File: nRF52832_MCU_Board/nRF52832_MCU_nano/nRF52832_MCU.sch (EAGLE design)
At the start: 17 parts, among them U1 NRF52832, X1 32MHz, X2 TSW-116-02-S-S, X3 TSW-116-02-S-S

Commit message: Finished? footprint and symbol for nRF5, QFN. Done som experimenting on board layouts
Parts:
- removed X2, X3: TSW-116-02-S-S, con-samtec:TSW-116-02-S-S
- added ANT1: 2.45GHZ_PCB_ANTENNA, nRF:2.45GHZ_PCB_ANTENNA
- added C13: 0.8pF, rcl:C-EUC0402
- added J1, J2: TSW-116-02-S-S, con-samtec:TSW-116-02-S-S
- X1: device IQD-Frequency-Products:CRYSTALS-GND-LID-IQXC-42 -> nRF:XTAL_32MHZ
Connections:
- net N$1 renamed ANT
- new net N$1: ANT1.P$1, C13.1, L1.2
- new net N$14: U1.SWDIO@26
- new net N$15: U1.SWDCLK@25
- new net P0.00: J1-1.1, U1.P0.00/XL1@02
- new net P0.01: J1-2.1, U1.P0.01/XL2@03
- new net P0.02: J1-3.1, U1.P0.02/AIN0@04
- new net P0.03: J1-4.1, U1.P0.03/AIN1@05
- new net P0.04: J1-5.1, U1.P0.04/AIN2@06
- new net P0.05: J1-6.1, U1.P0.05/AIN3@07
- new net P0.06: J1-7.1, U1.P0.06@08
- new net P0.07: J1-8.1, U1.P0.07@09
- new net P0.08: J1-9.1, U1.P0.08@10
- new net P0.09: J1-10.1, U1.P0.09@11
- new net P0.10: J1-11.1, U1.P0.10@12
- new net P0.11: J1-12.1, U1.P0.11@14
- new net P0.12: J1-13.1, U1.P0.12@15
- new net P0.13: J1-14.1, U1.P0.13@16
- new net P0.14: J1-15.1, U1.P0.14@17
- new net P0.15: J1-16.1, U1.P0.15@18
- new net P0.16: J2-16.1, U1.P0.16@19
- new net P0.17: J2-15.1, U1.P0.17@20
- new net P0.18: J2-14.1, U1.P0.18@21
- new net P0.19: J2-13.1, U1.P0.19@22
- new net P0.20: J2-12.1, U1.P0.20@23
- new net P0.21: J2-11.1, U1.P0.21/RESET@24
- new net P0.22: J2-10.1, U1.P0.22@27
- new net P0.23: J2-9.1, U1.P0.23@28
- new net P0.24: J2-8.1, U1.P0.24@29
- new net P0.25: J2-7.1, U1.P0.25@37
- new net P0.26: J2-6.1, U1.P0.26@38
- new net P0.27: J2-5.1, U1.P0.27@39
- new net P0.28: J2-4.1, U1.P0.28@40
- new net P0.29: J2-3.1, U1.P0.29@41
- new net P0.30: J2-2.1, U1.P0.30@42
- new net P0.31: J2-1.1, U1.P0.31@43
- net GND: now also C13.2

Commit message: Routed gpio
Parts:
- added C14, C15: 300pF, nRF:CAPACITOR_0402_N
- added C16: 100nF, nRF:CAPACITOR_0402_N
- added C17, C18: 10µF, nRF:CAPACITOR_0603_N
- added C19: 100µF, nRF:CAPACITOR_0805_N
- added C20: (no value), nRF:CAPACITOR_0402_N
- added J3: MM8130-2600, nRF:MM8130-2600
- added J4: FPC_05P-RA-SMD, nRF:FPC_05P-RA-SMD
- added J5: DEBUG_CONNECTOR, nRF:DEBUG_CONNECTOR
- added L2: 10µH, nRF:INDUCTOR_0603_N
- added L3: 15nH, nRF:INDUCTOR_0402_N
- added R1, R2, R3, R4: 0R, nRF:RESISTOR_0402_N
- added U$2: TLV1117, nRF:TLV1117
- added X2: 32.768kHz, nRF:XTAL_32KHZ
- ANT1: value 2.45GHZ_PCB_ANTENNA -> ANTENNA_QUARTER-WAVE_MONOPOLE_MEANDERED_LEFT; device nRF:2.45GHZ_PCB_ANTENNA -> nRF:ANTENNA_QUARTER-WAVE_MONOPOLE_MEANDERED_LEFT
- C1, C11, C12, C2, C3, C4, C5, C6, C7, C8: device rcl:C-EUC0402 -> nRF:CAPACITOR_0402_N
- C10, C9: device rcl:C-EUC0603 -> nRF:CAPACITOR_0603_N
- C13: value 0.8pF -> (none); device rcl:C-EUC0402 -> nRF:CAPACITOR_0402_N
- L1: device nRF:INDUCTOR(0402) -> nRF:INDUCTOR_0402_N
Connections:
- net N$4 renamed X1
- removed net N$14: U1.SWDIO@26
- removed net N$15: U1.SWDCLK@25
- removed net P0.18: J2-14.1, U1.P0.18@21
- removed net P0.21: J2-11.1, U1.P0.21/RESET@24
- removed net VCC: C5.1, C8.1, C9.1, U1.VDD@13, U1.VDD@36, U1.VDD@48
- new net N$2: L2.2, L3.1
- new net N$4: L2.1, U1.DCC@47
- new net N$5: C13.1, J3.@IN, L1.2
- new net NFC1: C14.2, J4.2, R3.1, U1.P0.09/NFC1@11
- new net NFC2: C15.1, J4.4, R4.2, U1.P0.10/NFC2@12
- new net P0.18/SWO: J1-10.1, J5.10, U1.P0.18/SWO@21
- new net P0.21/RESET: J1-13.1, J5.6, U1.P0.21/RESET@24
- new net SWDCLK: J5.4, U1.SWDCLK@25
- new net SWDIO: J5.2, U1.SWDIO@26
- new net VCC_P3V3: C18.1, C19.1, C5.1, C8.1, C9.1, J5.1, U$2.OUT, U1.VDD@13, U1.VDD@36, U1.VDD@48
- new net VCC_P5V0: C16.1, C17.1, U$2.IN
- new net XL1: C11.2, R1.1, U1.P0.00/XL1@02, X2.1
- new net XL2: C12.2, R2.2, U1.P0.01/XL2@03, X2.2
- net DEC4: now also L3.2
- net GND: now also C11.1, C12.1, C14.1, C15.2, C16.2, C17.2, C18.2, C19.2, C20.2, J3.@GND, J5.3, J5.5, J5.9, U$2.GND
- net N$1: now also C20.1, J3.@OUT; no longer C13.1, L1.2
- net P0.00: now also J2-9.1, R1.2; no longer J1-1.1, U1.P0.00/XL1@02
- net P0.01: now also J2-8.1, R2.1; no longer J1-2.1, U1.P0.01/XL2@03
- net P0.02: now also J2-7.1; no longer J1-3.1
- net P0.03: now also J2-6.1; no longer J1-4.1
- net P0.04: now also J2-5.1; no longer J1-5.1
- net P0.05: now also J2-4.1; no longer J1-6.1
- net P0.06: now also J2-3.1; no longer J1-7.1
- net P0.07: now also J2-2.1; no longer J1-8.1
- net P0.08: now also J2-1.1; no longer J1-9.1
- net P0.09: now also J1-1.1, R3.2; no longer J1-10.1, U1.P0.09@11
- net P0.10: now also J1-2.1, R4.1; no longer J1-11.1, U1.P0.10@12
- net P0.11: now also J1-3.1; no longer J1-12.1
- net P0.12: now also J1-4.1; no longer J1-13.1
- net P0.13: now also J1-5.1; no longer J1-14.1
- net P0.14: now also J1-6.1; no longer J1-15.1
- net P0.15: now also J1-7.1; no longer J1-16.1
- net P0.16: now also J1-8.1; no longer J2-16.1
- net P0.17: now also J1-9.1; no longer J2-15.1
- net P0.19: now also J1-11.1; no longer J2-13.1
- net P0.20: now also J1-12.1; no longer J2-12.1
- net P0.22: now also J1-14.1; no longer J2-10.1
- net P0.23: now also J1-15.1; no longer J2-9.1
- net P0.24: now also J1-16.1; no longer J2-8.1
- net P0.25: now also J2-16.1; no longer J2-7.1
- net P0.26: now also J2-15.1; no longer J2-6.1
- net P0.27: now also J2-14.1; no longer J2-5.1
- net P0.28: now also J2-13.1; no longer J2-4.1
- net P0.29: now also J2-12.1; no longer J2-3.1
- net P0.30: now also J2-11.1; no longer J2-2.1
- net P0.31: now also J2-10.1; no longer J2-1.1
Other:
- note added: "Power supply"

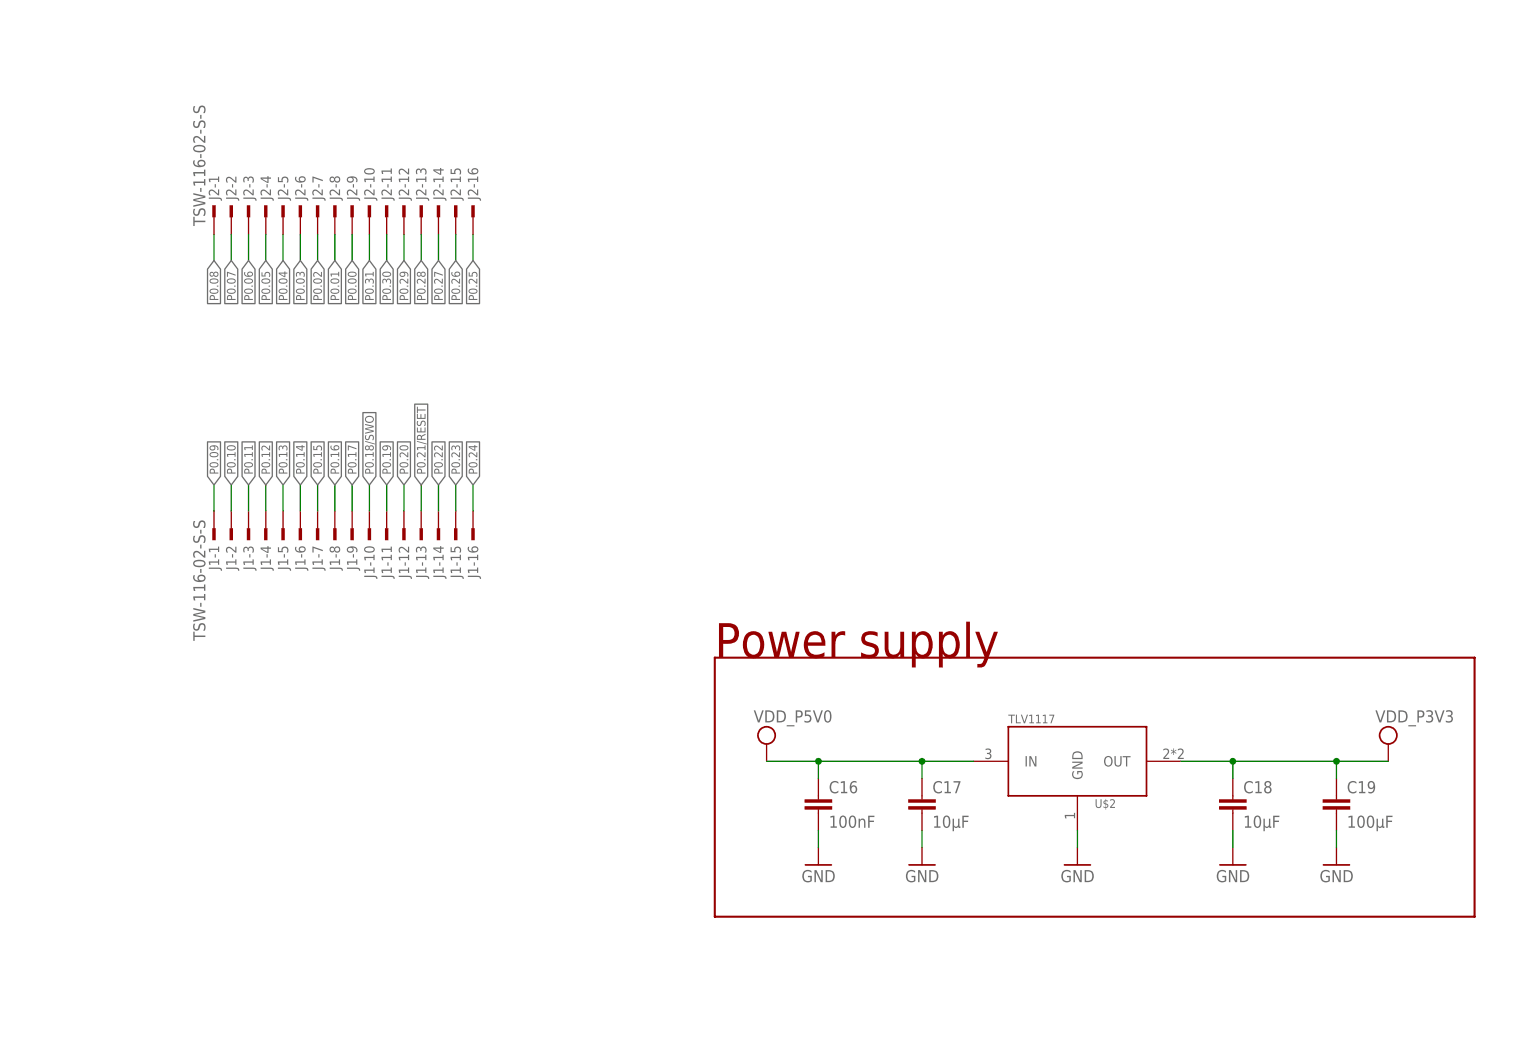
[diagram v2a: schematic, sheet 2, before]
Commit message: Positioned buttons, positioned powersupply
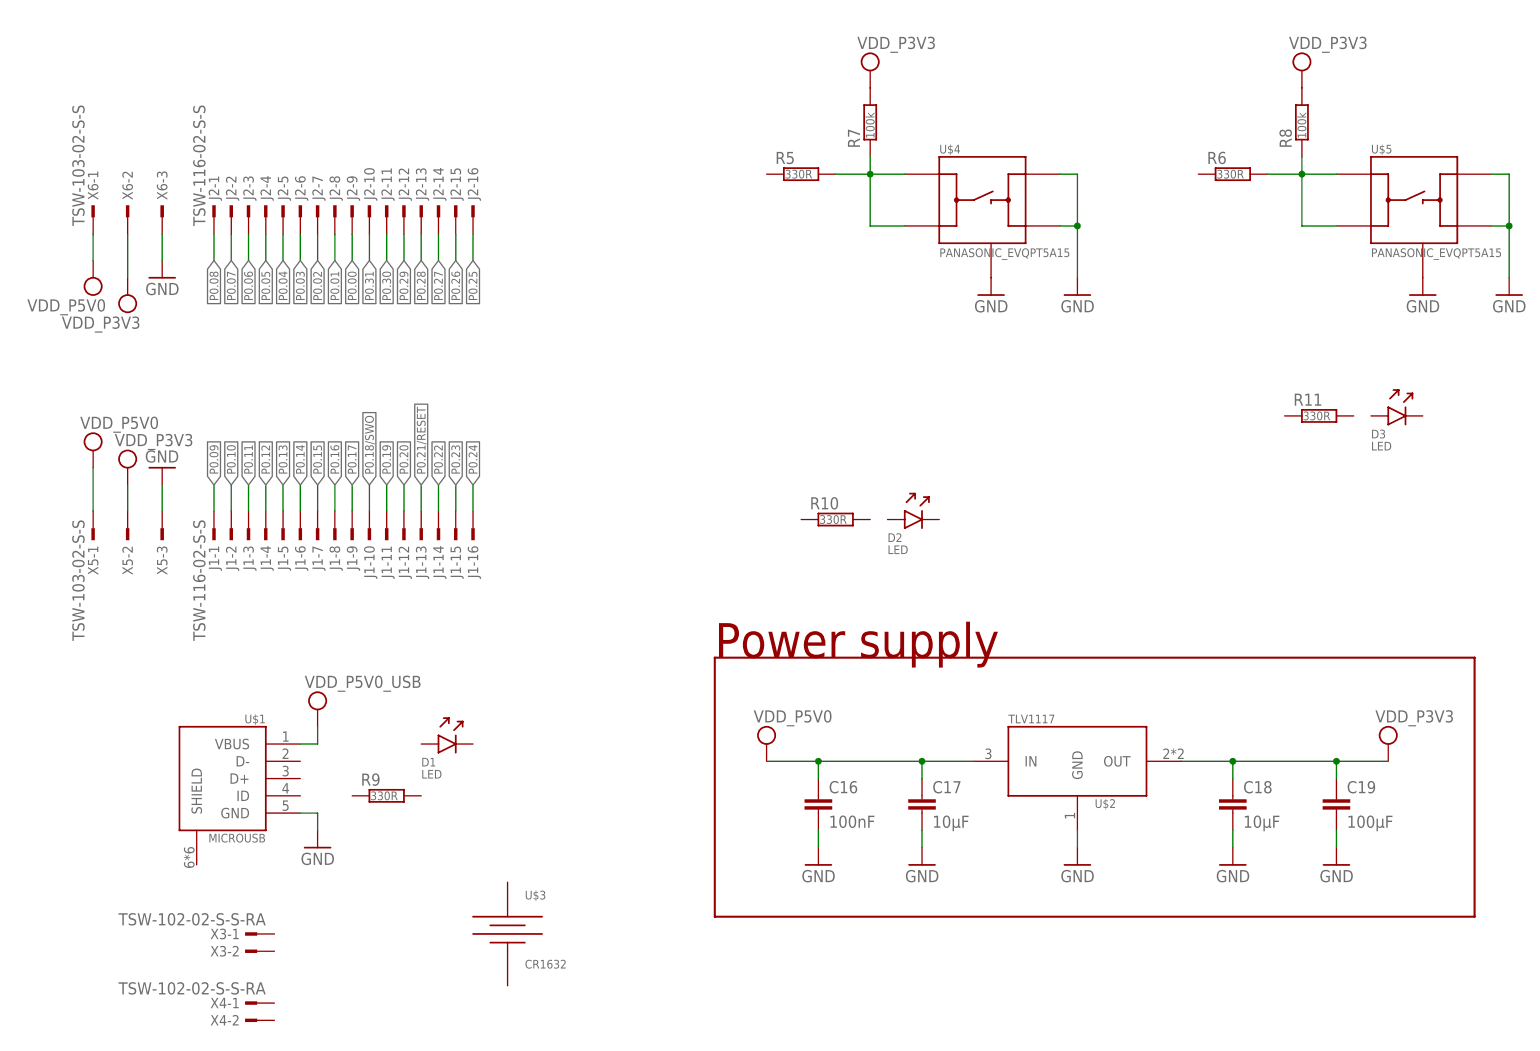
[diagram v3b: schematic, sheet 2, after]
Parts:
- added D1, D2, D3: LED, nRF:LED
- added R10, R11, R5, R6, R9: 330R, nRF:RESISTOR_0402_N
- added R7, R8: 100k, nRF:RESISTOR_0402_N
- added U$1: MICROUSB, nRF:MICROUSB
- added U$3: CR1632, nRF:CR1632
- added U$4, U$5: PANASONIC_EVQPT5A15, nRF:PANASONIC_EVQPT5A15
- added X3, X4: TSW-102-02-S-S-RA, con-samtec:TSW-102-02-S-S-RA
- added X5, X6: TSW-103-02-S-S, con-samtec:TSW-103-02-S-S
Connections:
- new net N$6: R6.2, R8.1, U$5.A, U$5.A'
- new net N$7: R5.2, R7.1, U$4.A, U$4.A'
- new net VCC: R7.2, R8.2
- new net VCC_P5V0_USB: U$1.VBUS
- net GND: now also U$1.GND, U$4.B, U$4.B', U$4.GND, U$5.B, U$5.B', U$5.GND, X5-3.1, X6-3.1
- net VCC_P3V3: now also X5-2.1, X6-2.1
- net VCC_P5V0: now also X5-1.1, X6-1.1
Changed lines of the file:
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@@
 <part name="C11" library="nRF" deviceset="CAPACITOR" device="_0402_N" value="12pF"/>
 <part name="C12" library="nRF" deviceset="CAPACITOR" device="_0402_N" value="12pF"/>
+<part name="U$1" library="nRF" deviceset="MICROUSB" device=""/>
+<part name="VDD_NRF6" library="supply2" deviceset="VCC" device="" value="VDD_P5V0_USB"/>
+<part name="GND22" library="supply1" deviceset="GND" device=""/>
+<part name="X3" library="con-samtec" deviceset="TSW-102-02-S-S" device="-RA"/>
+<part name="X4" library="con-samtec" deviceset="TSW-102-02-S-S" device="-RA"/>
+<part name="X5" library="con-samtec" deviceset="TSW-103-02-S-S" device=""/>
+<part name="X6" library="con-samtec" deviceset="TSW-103-02-S-S" device=""/>
+<part name="VDD_NRF7" library="supply2" deviceset="VCC" device="" value="VDD_P5V0"/>
+<part name="VDD_NRF8" library="supply2" deviceset="VCC" device="" value="VDD_P3V3"/>
+<part name="GND23" library="supply1" deviceset="GND" device=""/>
+<part name="VDD_NRF9" library="supply2" deviceset="VCC" device="" value="VDD_P5V0"/>
+<part name="VDD_NRF10" library="supply2" deviceset="VCC" device="" value="VDD_P3V3"/>
+<part name="GND24" library="supply1" deviceset="GND" device=""/>
+<part name="U$3" library="nRF" deviceset="CR1632" device=""/>
+<part name="U$4" library="nRF" deviceset="PANASONIC_EVQPT5A15" device=""/>
+<part name="U$5" library="nRF" deviceset="PANASONIC_EVQPT5A15" device=""/>
+<part name="R7" library="nRF" deviceset="RESISTOR" device="_0402_N" value="100k"/>
+<part name="R8" library="nRF" deviceset="RESISTOR" device="_0402_N" value="100k"/>
+<part name="VDD_NRF11" library="supply2" deviceset="VCC" device="" value="VDD_P3V3"/>
+<part name="VDD_NRF12" library="supply2" deviceset="VCC" device="" value="VDD_P3V3"/>
+<part name="GND25" library="supply1" deviceset="GND" device=""/>
+<part name="GND26" library="supply1" deviceset="GND" device=""/>
+<part name="GND27" library="supply1" deviceset="GND" device=""/>
+<part name="GND28" library="supply1" deviceset="GND" device=""/>
+<part name="R5" library="nRF" deviceset="RESISTOR" device="_0402_N" value="330R"/>
+<part name="R6" library="nRF" deviceset="RESISTOR" device="_0402_N" value="330R"/>
+<part name="D1" library="nRF" deviceset="LED" device=""/>
+<part name="D3" library="nRF" deviceset="LED" device=""/>
+<part name="D2" library="nRF" deviceset="LED" device=""/>
+<part name="R9" library="nRF" deviceset="RESISTOR" device="_0402_N" value="330R"/>
+<part name="R10" library="nRF" deviceset="RESISTOR" device="_0402_N" value="330R"/>
+<part name="R11" library="nRF" deviceset="RESISTOR" device="_0402_N" value="330R"/>
 </parts>
 <sheets>
@@
 <instance part="GND19" gate="1" x="203.2" y="40.64" rot="MR0"/>
 <instance part="GND20" gate="1" x="218.44" y="40.64" rot="MR0"/>
+<instance part="U$1" gate="G$1" x="60.96" y="45.72" rot="MR0"/>
+<instance part="VDD_NRF6" gate="G$1" x="68.58" y="63.5"/>
+<instance part="GND22" gate="1" x="68.58" y="43.18" rot="MR0"/>
+<instance part="X3" gate="-1" x="59.69" y="30.48" rot="MR0"/>
+<instance part="X3" gate="-2" x="59.69" y="27.94" rot="MR0"/>
+<instance part="X4" gate="-1" x="59.69" y="20.32" rot="MR0"/>
+<instance part="X4" gate="-2" x="59.69" y="17.78" rot="MR0"/>
+<instance part="X5" gate="-1" x="35.56" y="90.17" rot="MR270"/>
+<instance part="X5" gate="-2" x="40.64" y="90.17" rot="MR270"/>
+<instance part="X5" gate="-3" x="45.72" y="90.17" rot="MR270"/>
+<instance part="X6" gate="-1" x="35.56" y="135.89" rot="R90"/>
+<instance part="X6" gate="-2" x="40.64" y="135.89" rot="R90"/>
+<instance part="X6" gate="-3" x="45.72" y="135.89" rot="R90"/>
+<instance part="VDD_NRF7" gate="G$1" x="35.56" y="101.6"/>
+<instance part="VDD_NRF8" gate="G$1" x="40.64" y="99.06"/>
+<instance part="GND23" gate="1" x="45.72" y="99.06" rot="MR180"/>
+<instance part="VDD_NRF9" gate="G$1" x="35.56" y="127" rot="R180"/>
+<instance part="VDD_NRF10" gate="G$1" x="40.64" y="124.46" rot="R180"/>
+<instance part="GND24" gate="1" x="45.72" y="127" rot="MR0"/>
+<instance part="U$3" gate="G$1" x="96.52" y="30.48"/>
+<instance part="U$4" gate="G$1" x="160.02" y="132.08"/>
+<instance part="U$5" gate="G$1" x="223.52" y="132.08"/>
+<instance part="R7" gate="R$1" x="149.86" y="149.86" rot="R90"/>
+<instance part="R8" gate="R$1" x="213.36" y="149.86" rot="R90"/>
+<instance part="VDD_NRF11" gate="G$1" x="213.36" y="157.48"/>
+<instance part="VDD_NRF12" gate="G$1" x="149.86" y="157.48"/>
+<instance part="GND25" gate="1" x="167.64" y="124.46" rot="MR0"/>
+<instance part="GND26" gate="1" x="180.34" y="124.46" rot="MR0"/>
+<instance part="GND27" gate="1" x="231.14" y="124.46" rot="MR0"/>
+<instance part="GND28" gate="1" x="243.84" y="124.46" rot="MR0"/>
+<instance part="R5" gate="R$1" x="139.7" y="142.24"/>
+<instance part="R6" gate="R$1" x="203.2" y="142.24"/>
+<instance part="D1" gate="D$1" x="88.9" y="58.42"/>
+<instance part="D3" gate="D$1" x="228.6" y="106.68"/>
+<instance part="D2" gate="D$1" x="157.48" y="91.44"/>
+<instance part="R9" gate="R$1" x="78.74" y="50.8"/>
+<instance part="R10" gate="R$1" x="144.78" y="91.44"/>
+<instance part="R11" gate="R$1" x="215.9" y="106.68"/>
 </instances>
 <busses>
@@
 <junction x="218.44" y="55.88"/>
 </segment>
+<segment>
+<pinref part="VDD_NRF8" gate="G$1" pin="VCC"/>
+<pinref part="X5" gate="-2" pin="1"/>
+<wire x1="40.64" y1="96.52" x2="40.64" y2="92.71" width="0.1524" layer="91"/>
+</segment>
+<segment>
+<pinref part="VDD_NRF10" gate="G$1" pin="VCC"/>
+<pinref part="X6" gate="-2" pin="1"/>
+<wire x1="40.64" y1="127" x2="40.64" y2="133.35" width="0.1524" layer="91"/>
+</segment>
 </net>
 <net name="GND" class="0">
@@
 <pinref part="C19" gate="C$1" pin="2"/>
 <wire x1="218.44" y1="43.18" x2="218.44" y2="45.72" width="0.1524" layer="91"/>
+</segment>
+<segment>
+<pinref part="U$1" gate="G$1" pin="GND"/>
+<pinref part="GND22" gate="1" pin="GND"/>
+<wire x1="66.04" y1="48.26" x2="68.58" y2="48.26" width="0.1524" layer="91"/>
+<wire x1="68.58" y1="48.26" x2="68.58" y2="45.72" width="0.1524" layer="91"/>
+</segment>
+<segment>
+<pinref part="GND23" gate="1" pin="GND"/>
+<pinref part="X5" gate="-3" pin="1"/>
+<wire x1="45.72" y1="96.52" x2="45.72" y2="92.71" width="0.1524" layer="91"/>
+</segment>
+<segment>
+<pinref part="GND24" gate="1" pin="GND"/>
+<pinref part="X6" gate="-3" pin="1"/>
+<wire x1="45.72" y1="129.54" x2="45.72" y2="133.35" width="0.1524" layer="91"/>
+</segment>
+<segment>
+<pinref part="U$4" gate="G$1" pin="GND"/>
+<pinref part="GND25" gate="1" pin="GND"/>
+</segment>
+<segment>
+<pinref part="U$4" gate="G$1" pin="B"/>
+<wire x1="177.8" y1="142.24" x2="180.34" y2="142.24" width="0.1524" layer="91"/>
+<wire x1="180.34" y1="142.24" x2="180.34" y2="134.62" width="0.1524" layer="91"/>
+<pinref part="U$4" gate="G$1" pin="B'"/>
+<wire x1="180.34" y1="134.62" x2="180.34" y2="127" width="0.1524" layer="91"/>
+<wire x1="177.8" y1="134.62" x2="180.34" y2="134.62" width="0.1524" layer="91"/>
+<junction x="180.34" y="134.62"/>
+<pinref part="GND26" gate="1" pin="GND"/>
+</segment>
+<segment>
+<pinref part="U$5" gate="G$1" pin="GND"/>
+<pinref part="GND27" gate="1" pin="GND"/>
+</segment>
+<segment>
+<pinref part="U$5" gate="G$1" pin="B"/>
+<wire x1="241.3" y1="142.24" x2="243.84" y2="142.24" width="0.1524" layer="91"/>
+<wire x1="243.84" y1="142.24" x2="243.84" y2="134.62" width="0.1524" layer="91"/>
+<pinref part="U$5" gate="G$1" pin="B'"/>
+<wire x1="243.84" y1="134.62" x2="243.84" y2="127" width="0.1524" layer="91"/>
+<wire x1="241.3" y1="134.62" x2="243.84" y2="134.62" width="0.1524" layer="91"/>
+<junction x="243.84" y="134.62"/>
+<pinref part="GND28" gate="1" pin="GND"/>
 </segment>
 </net>
@@
 <junction x="157.48" y="55.88"/>
 </segment>
-</net>
+<segment>
+<pinref part="VDD_NRF7" gate="G$1" pin="VCC"/>
+<pinref part="X5" gate="-1" pin="1"/>
+<wire x1="35.56" y1="99.06" x2="35.56" y2="92.71" width="0.1524" layer="91"/>
+</segment>
+<segment>
+<pinref part="VDD_NRF9" gate="G$1" pin="VCC"/>
+<pinref part="X6" gate="-1" pin="1"/>
+<wire x1="35.56" y1="129.54" x2="35.56" y2="133.35" width="0.1524" layer="91"/>
+</segment>
+</net>
+<net name="VCC_P5V0_USB" class="0">
+<segment>
+<pinref part="U$1" gate="G$1" pin="VBUS"/>
+<pinref part="VDD_NRF6" gate="G$1" pin="VCC"/>
+<wire x1="66.04" y1="58.42" x2="68.58" y2="58.42" width="0.1524" layer="91"/>
+<wire x1="68.58" y1="58.42" x2="68.58" y2="60.96" width="0.1524" layer="91"/>
+</segment>
+</net>
+<net name="VCC" class="0">
+<segment>
+<pinref part="R8" gate="R$1" pin="2"/>
+<pinref part="VDD_NRF11" gate="G$1" pin="VCC"/>
+</segment>
+<segment>
+<pinref part="R7" gate="R$1" pin="2"/>
+<pinref part="VDD_NRF12" gate="G$1" pin="VCC"/>
+</segment>
+</net>
+<net name="N$6" class="0">
+<segment>
+<pinref part="U$5" gate="G$1" pin="A'"/>
+<pinref part="R8" gate="R$1" pin="1"/>
+<wire x1="218.44" y1="134.62" x2="213.36" y2="134.62" width="0.1524" layer="91"/>
+<wire x1="213.36" y1="134.62" x2="213.36" y2="142.24" width="0.1524" layer="91"/>
+<pinref part="U$5" gate="G$1" pin="A"/>
+<wire x1="213.36" y1="142.24" x2="213.36" y2="144.78" width="0.1524" layer="91"/>
+<wire x1="218.44" y1="142.24" x2="213.36" y2="142.24" width="0.1524" layer="91"/>
+<junction x="213.36" y="142.24"/>
+<pinref part="R6" gate="R$1" pin="2"/>
+<wire x1="213.36" y1="142.24" x2="208.28" y2="142.24" width="0.1524" layer="91"/>
+</segment>
+</net>
+<net name="N$7" class="0">
+<segment>
+<pinref part="U$4" gate="G$1" pin="A'"/>
+<pinref part="R7" gate="R$1" pin="1"/>
+<wire x1="154.94" y1="134.62" x2="149.86" y2="134.62" width="0.1524" layer="91"/>
+<wire x1="149.86" y1="134.62" x2="149.86" y2="142.24" width="0.1524" layer="91"/>
+<pinref part="U$4" gate="G$1" pin="A"/>
+<wire x1="149.86" y1="142.24" x2="149.86" y2="144.78" width="0.1524" layer="91"/>
+<wire x1="154.94" y1="142.24" x2="149.86" y2="142.24" width="0.1524" layer="91"/>
+<junction x="149.86" y="142.24"/>
+<pinref part="R5" gate="R$1" pin="2"/>
+<wire x1="149.86" y1="142.24" x2="144.78" y2="142.24" width="0.1524" layer="91"/>
+</segment>
+</net>
